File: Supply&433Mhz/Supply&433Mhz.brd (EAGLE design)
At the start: 65 x 56.5 mm, 17 parts, among them K1 61004021821, P1 DF11-06-2DSA, Q1 BS170

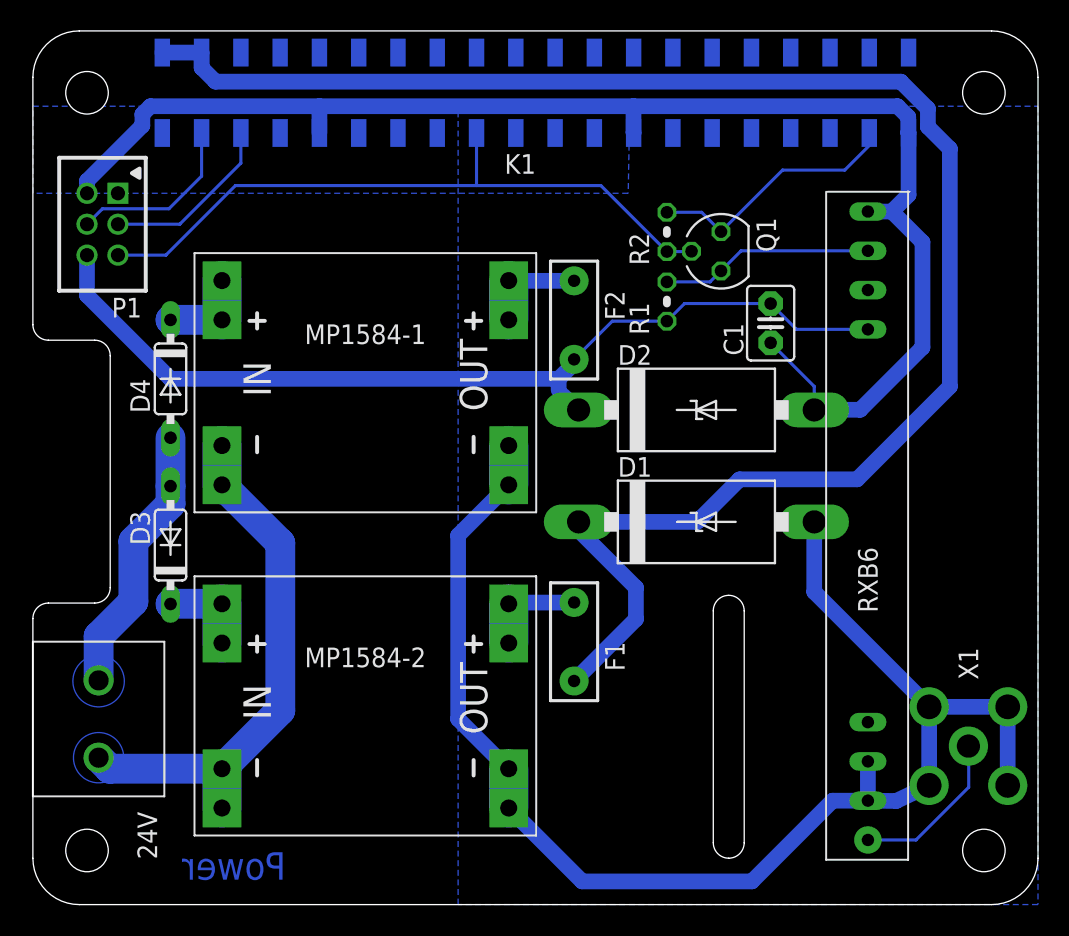
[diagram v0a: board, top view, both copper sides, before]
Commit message: Remove AGND supply, since DC/DC converter use same GND signal.
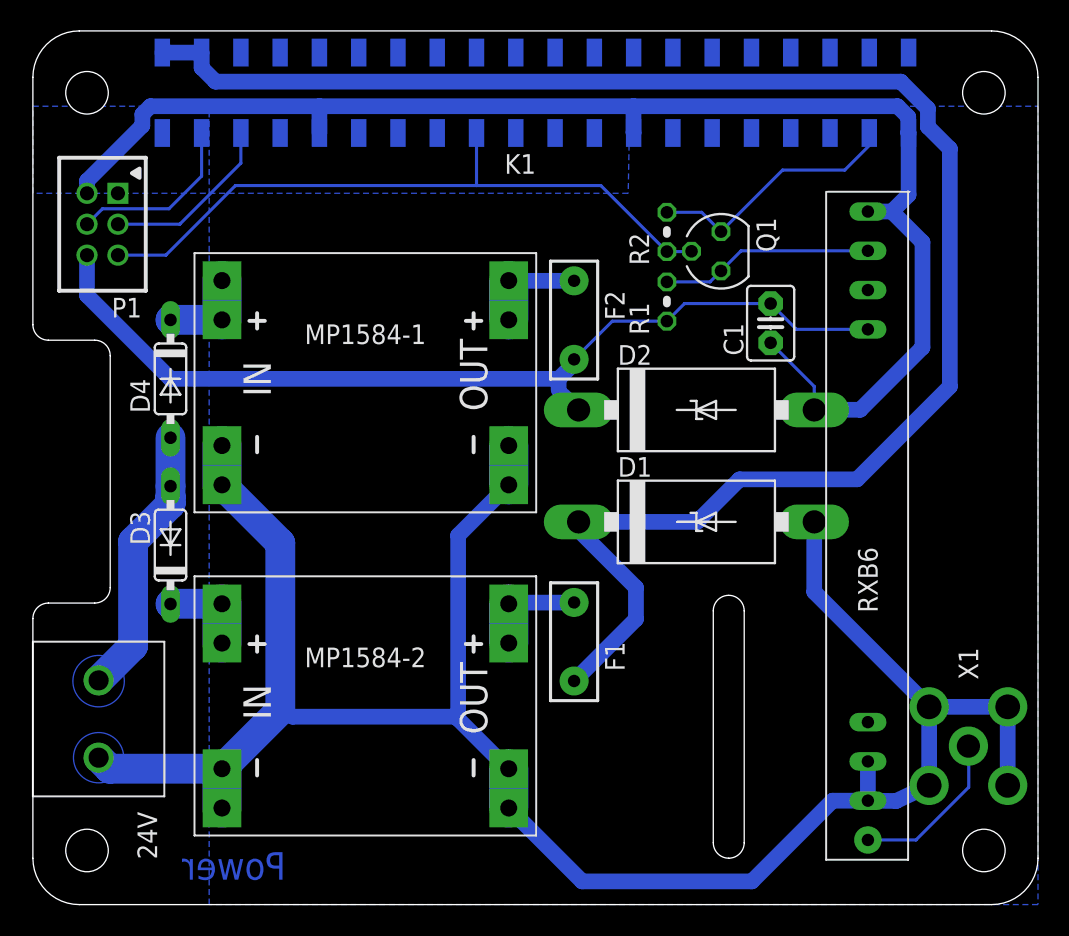
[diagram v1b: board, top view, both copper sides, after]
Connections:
- removed net AGND: 24V.1, MP1584-1.IN-0, MP1584-1.IN-1, MP1584-2.IN-0, MP1584-2.IN-1
- net GND: now also 24V.1, MP1584-1.IN-0, MP1584-1.IN-1, MP1584-2.IN-0, MP1584-2.IN-1
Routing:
- net GND: track 182.5 -> 229.3 mm
- net AGND: track 35.1 -> 0.00 mm
- net +24V: track 17.6 -> 18.1 mm
- removed copper zone on layer 16, net AGND
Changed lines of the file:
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@@
 <contactref element="MP1584-1" pad="OUT-0"/>
 <polygon width="1.016" layer="16" isolate="0.4064" thermals="no">
-<vertex x="27.5" y="0"/>
-<vertex x="27.5" y="51.63"/>
+<vertex x="11.4" y="0"/>
+<vertex x="11.4" y="51.63"/>
 <vertex x="65" y="51.63"/>
 <vertex x="65" y="0"/>
@@
 <vertex x="0" y="51.63"/>
 </polygon>
-</signal>
-<signal name="+24V">
-<contactref element="D3" pad="A"/>
-<contactref element="D4" pad="A"/>
-<contactref element="24V" pad="2"/>
-<polygon width="0.35" layer="16" isolate="0.254" thermals="no">
-<vertex x="3.15" y="13.2" curve="180"/>
-<vertex x="5.35" y="15.7" curve="180"/>
-</polygon>
-<wire x1="4.25" y1="17.35" x2="6.5" y2="19.6" width="1.9304" layer="16"/>
-<wire x1="6.5" y1="19.6" x2="6.5" y2="23.5" width="1.9304" layer="16"/>
-<wire x1="6.5" y1="23.5" x2="8.9" y2="25.9" width="1.9304" layer="16"/>
-<wire x1="8.9" y1="25.9" x2="8.9" y2="27.06" width="1.9304" layer="16"/>
-<wire x1="4.25" y1="14.5" x2="4.25" y2="17.35" width="1.9304" layer="16"/>
-<wire x1="8.9" y1="30.19" x2="8.9" y2="27.06" width="1.9304" layer="16"/>
-</signal>
-<signal name="AGND">
 <contactref element="MP1584-2" pad="IN-0"/>
 <contactref element="MP1584-1" pad="IN-0"/>
 <contactref element="24V" pad="1"/>
-<polygon width="0.35" layer="16" thermals="no">
-<vertex x="3.15" y="8.3" curve="180"/>
-<vertex x="5.35" y="10.7" curve="180"/>
-</polygon>
 <contactref element="MP1584-2" pad="IN-1"/>
 <contactref element="MP1584-1" pad="IN-1"/>
@@
 <wire x1="12.229" y1="27.146" x2="16" y2="23.375" width="1.9304" layer="16"/>
 <wire x1="16" y1="23.375" x2="16" y2="12.557" width="1.9304" layer="16"/>
+<wire x1="27.1624" y1="12.1516" x2="16.7978" y2="12.1516" width="1.016" layer="16"/>
+<wire x1="16.7978" y1="12.1516" x2="16" y2="12.557" width="1.016" layer="16"/>
+<wire x1="27.1624" y1="12.1516" x2="27.5" y2="12" width="0.1524" layer="16"/>
+<polygon width="0.35" layer="16" thermals="no">
+<vertex x="3.15" y="8.3" curve="180"/>
+<vertex x="5.35" y="10.7" curve="180"/>
+</polygon>
+</signal>
+<signal name="+24V">
+<contactref element="D3" pad="A"/>
+<contactref element="D4" pad="A"/>
+<contactref element="24V" pad="2"/>
+<polygon width="0.35" layer="16" isolate="0.254" thermals="no">
+<vertex x="3.15" y="13.2" curve="180"/>
+<vertex x="5.35" y="15.7" curve="180"/>
+</polygon>
+<wire x1="8.9" y1="25.9" x2="8.9" y2="26.4" width="1.9304" layer="16"/>
+<wire x1="8.9" y1="26.4" x2="8.9" y2="27.06" width="1.9304" layer="16"/>
+<wire x1="8.9" y1="30.19" x2="8.9" y2="27.06" width="1.9304" layer="16"/>
+<wire x1="4.25" y1="14.5" x2="6.48" y2="16.73" width="1.9304" layer="16"/>
+<wire x1="6.48" y1="16.73" x2="6.48" y2="23.48" width="1.9304" layer="16"/>
+<wire x1="6.48" y1="23.48" x2="8.9" y2="25.9" width="1.9304" layer="16"/>
+<wire x1="8.9" y1="25.9" x2="8.9" y2="26.4" width="1.9304" layer="16"/>
 </signal>
 <signal name="N$2">

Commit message: Remove Schottky - Diodes, since already on DC/DC buck converter.
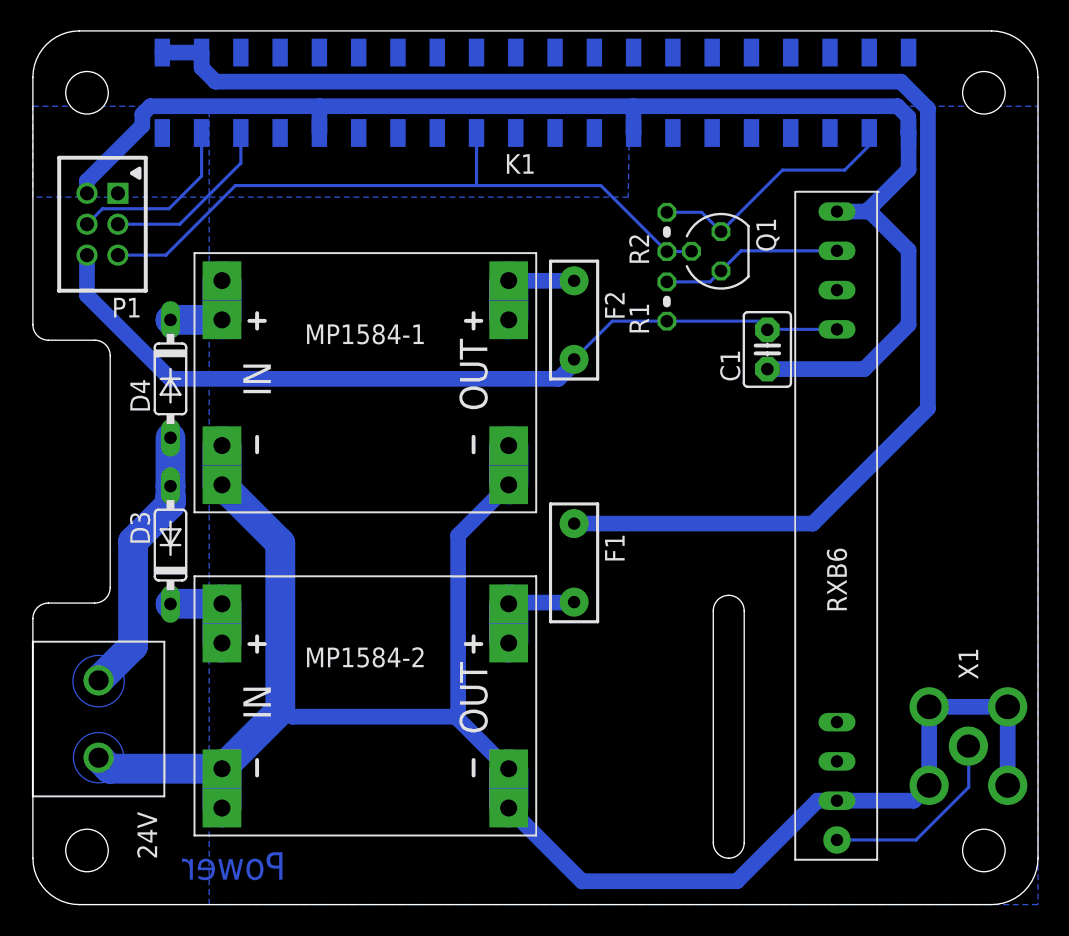
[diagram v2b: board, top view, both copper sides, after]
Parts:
- removed D1, D2: 1N5908, diode:C4111-15
- moved F1 5.10 mm to (35.0, 22.1), turned to 270 degrees
- moved RXB6 2.00 mm to (52.0, 24.5)
- moved C1 1.71 mm to (47.5, 35.9)
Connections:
- net GND: no longer D1.A, D2.A
- net N$2: no longer D2.C
- net N$5: no longer D1.C
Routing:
- net GND: track 229.3 -> 208.0 mm
- net N$5: track 111.3 -> 96.9 mm
- net N$2: track 60.8 -> 55.3 mm
- net N$8: track 10.6 -> 12.6 mm
- net N$3: track 13.8 -> 11.8 mm

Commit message: Revert "Remove Schottky - Diodes, since already on DC/DC buck converter."
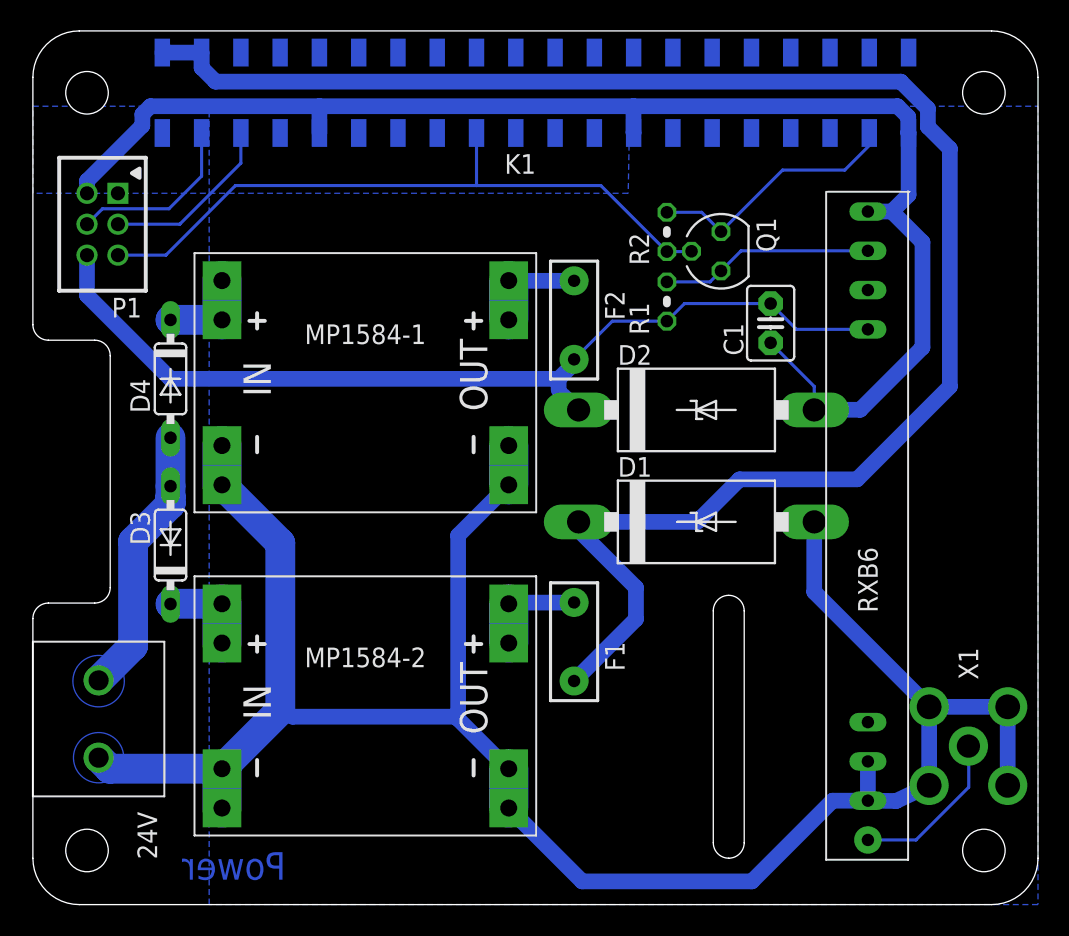
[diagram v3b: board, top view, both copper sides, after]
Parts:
- added D1, D2: 1N5908, diode:C4111-15
- moved F1 5.10 mm to (35.0, 17.0), turned to 90 degrees
- moved RXB6 2.00 mm to (54.0, 24.5)
- moved C1 1.71 mm to (47.7, 37.6)
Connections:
- net GND: now also D1.A, D2.A
- net N$2: now also D2.C
- net N$5: now also D1.C
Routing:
- net GND: track 208.0 -> 229.3 mm
- net N$5: track 96.9 -> 111.3 mm
- net N$2: track 55.3 -> 60.8 mm
- net N$8: track 12.6 -> 10.6 mm
- net N$3: track 11.8 -> 13.8 mm

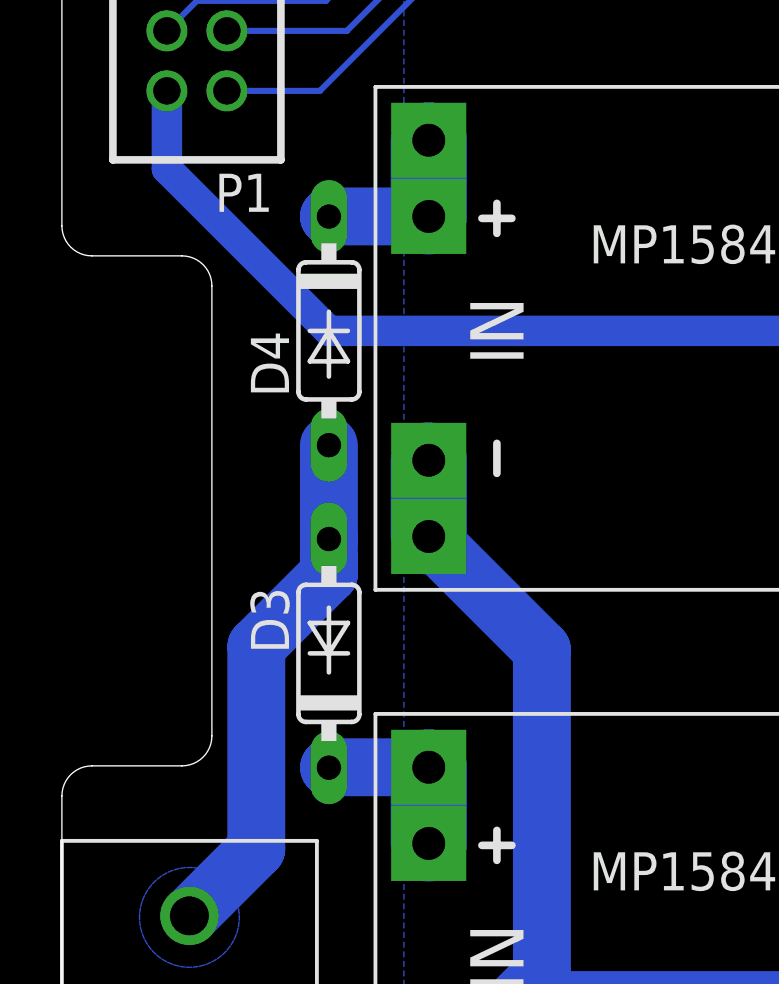
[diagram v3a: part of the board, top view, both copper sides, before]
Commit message: Change protection diode from 1N4148 to BS160.
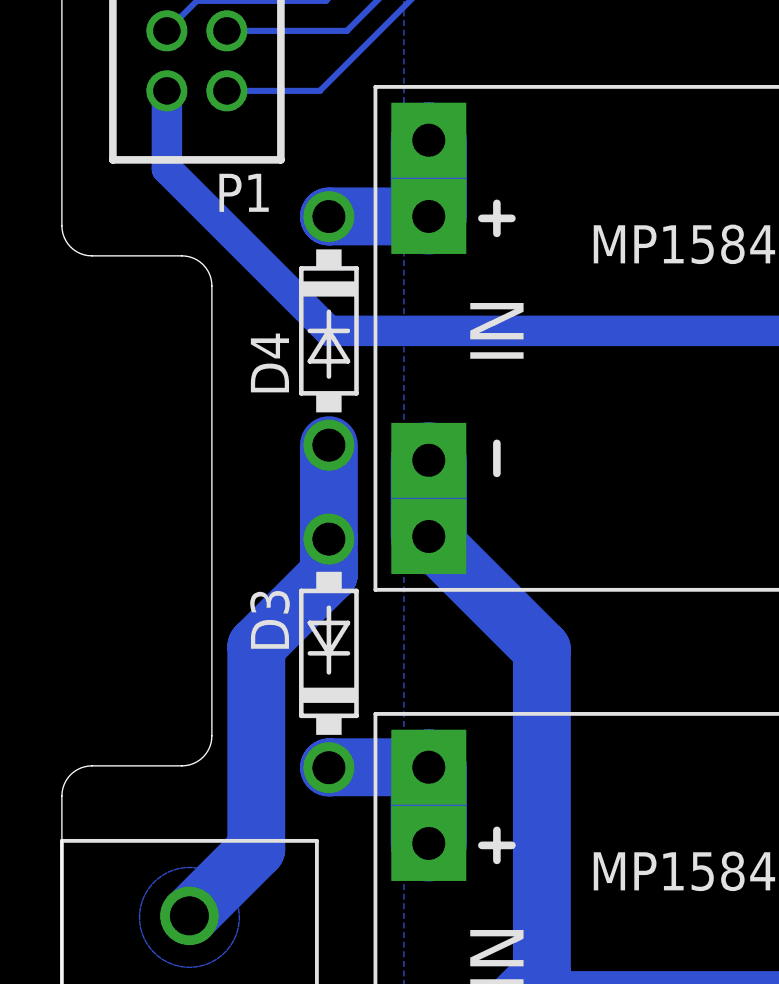
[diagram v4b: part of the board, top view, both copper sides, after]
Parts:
- D3, D4: value 1N4148DO35-7 -> SB160; device diode:DO35-7 -> diode:DO41-7.6
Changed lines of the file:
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@@
 <attribute name="VALUE" x="21.5" y="31.55" size="1.27" layer="27" align="top-center"/>
 </element>
-<element name="D3" library="diode" package="DO35-7" value="1N4148DO35-7" x="8.9" y="23.25" smashed="yes" rot="R90">
+<element name="D3" library="diode" package="DO41-7.6" value="SB160" x="8.9" y="23.25" smashed="yes" rot="R90">
 <attribute name="NAME" x="6.3" y="23.25" size="1.27" layer="25" font="vector" ratio="10" rot="R90" align="top-left"/>
 <attribute name="VALUE" x="11.567" y="20.964" size="1.27" layer="27" ratio="10" rot="R90"/>
 </element>
-<element name="D4" library="diode" package="DO35-7" value="1N4148DO35-7" x="8.9" y="34" smashed="yes" rot="R270">
+<element name="D4" library="diode" package="DO41-7.6" value="SB160" x="8.9" y="34" smashed="yes" rot="R270">
 <attribute name="NAME" x="6.3" y="34" size="1.27" layer="25" font="vector" ratio="10" rot="R270"/>
 <attribute name="VALUE" x="6.233" y="36.286" size="1.27" layer="27" ratio="10" rot="R270"/>

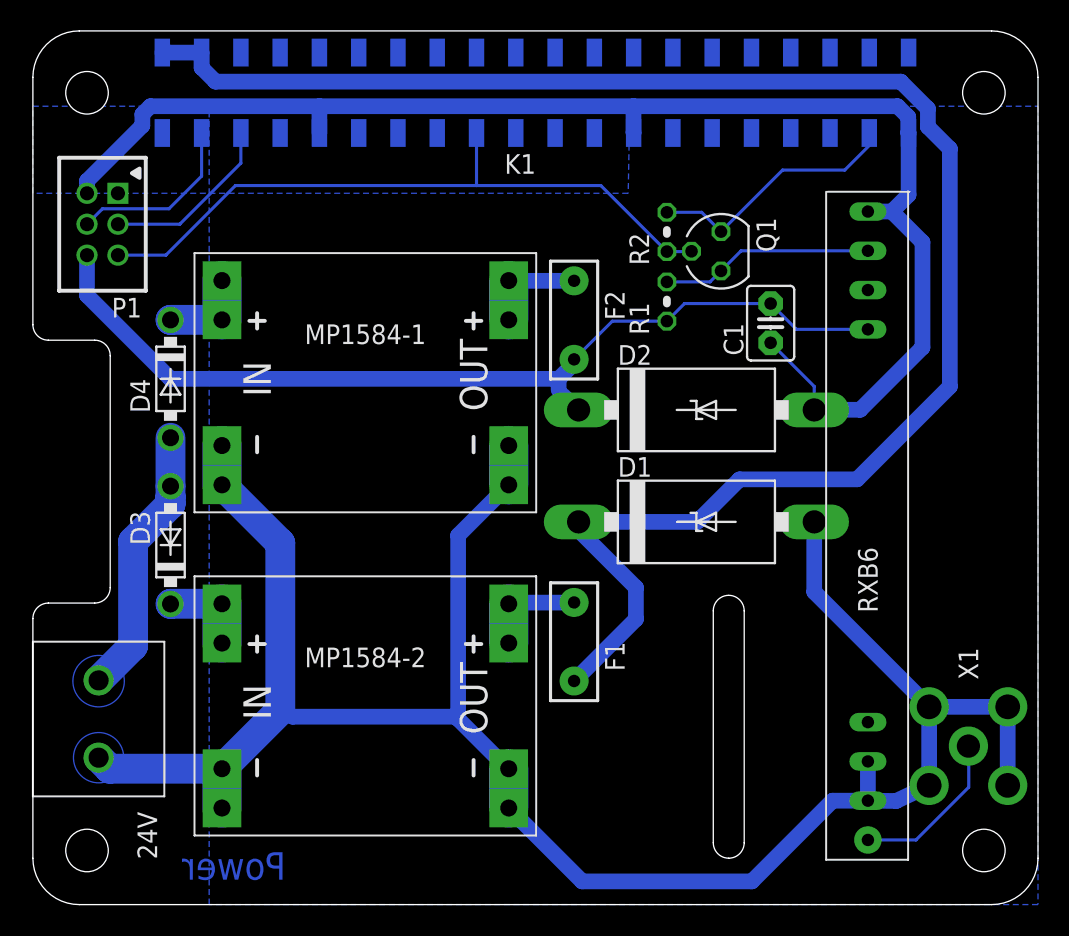
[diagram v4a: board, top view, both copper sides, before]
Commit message: Increase ground plane.
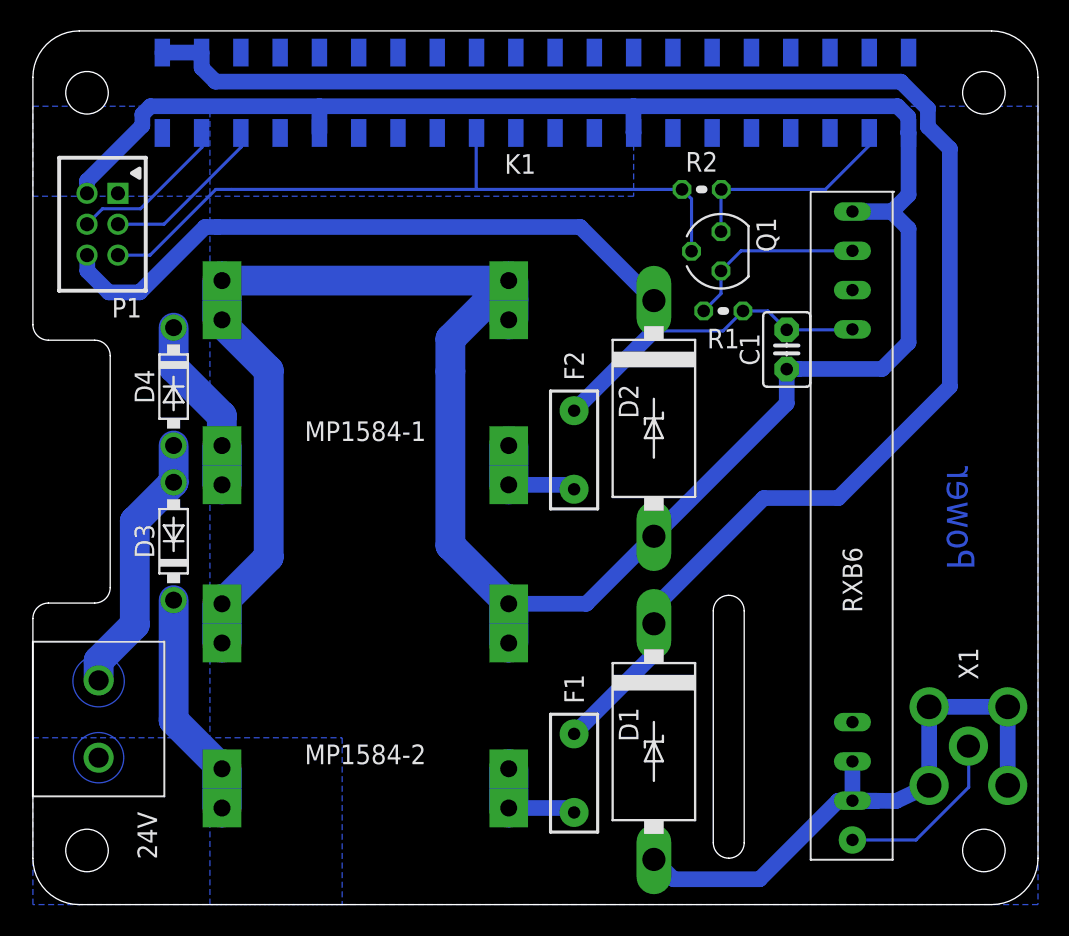
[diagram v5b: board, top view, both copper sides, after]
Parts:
- moved D1 14.5 mm to (40.2, 10.5), turned to 270 degrees
- moved F1 8.50 mm to (35.0, 8.50), turned to 270 degrees
- moved F2 8.40 mm to (35.0, 29.4), turned to 90 degrees
- moved R1 3.70 mm to (44.6, 38.4), turned to 180 degrees
- moved R2 3.55 mm to (43.2, 46.2), turned to 180 degrees
- moved D2 2.80 mm to (40.2, 31.4), turned to 270 degrees
- moved C1 1.99 mm to (48.8, 35.9)
- moved RXB6 1.00 mm to (53.0, 24.5)
- moved D4 0.54 mm to (9.10, 33.5)
- moved D3 0.32 mm to (9.10, 23.5)
- flipped MP1584-1 to the bottom, turned to 180 degrees
- flipped MP1584-2 to the bottom, turned to 180 degrees
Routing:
- net N$7: track 5.89 -> 14.8 mm
- net N$5: track 111.3 -> 105.5 mm
- net N$9: track 5.87 -> 11.5 mm
- net N$2: track 60.8 -> 65.1 mm
- net N$69: track 16.7 -> 14.3 mm
- net N$11: track 44.3 -> 46.3 mm
- net N$3: track 13.8 -> 12.1 mm
- net N$12: track 11.5 -> 10.4 mm
- net N$8: track 10.6 -> 11.6 mm
- net +24V: track 18.1 -> 17.2 mm
- net GND: track 229.3 -> 228.5 mm
- net N$1: track 11.5 -> 11.0 mm
